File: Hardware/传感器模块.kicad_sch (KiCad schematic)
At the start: 1 part, among them U2 AHT20

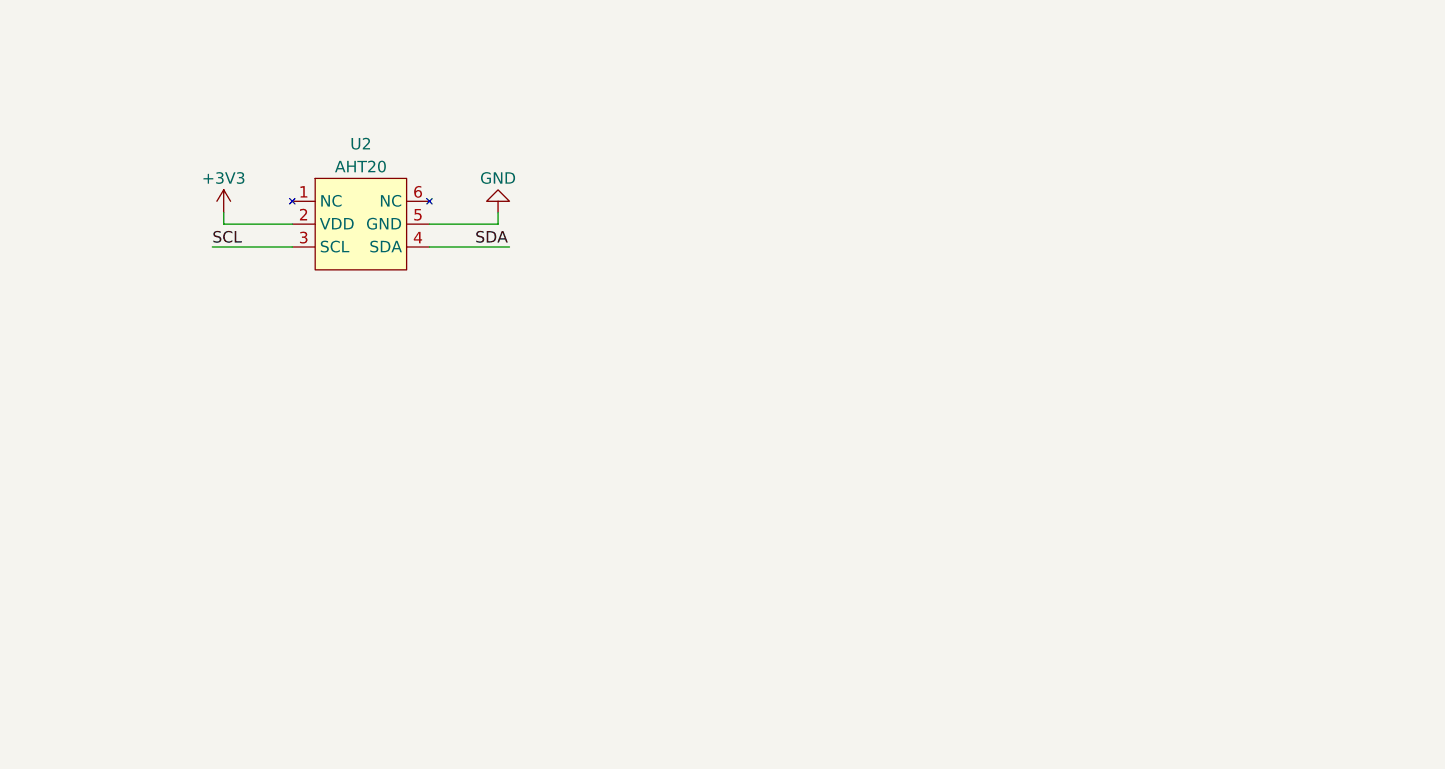
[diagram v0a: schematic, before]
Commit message: 完成传感器模块原理图
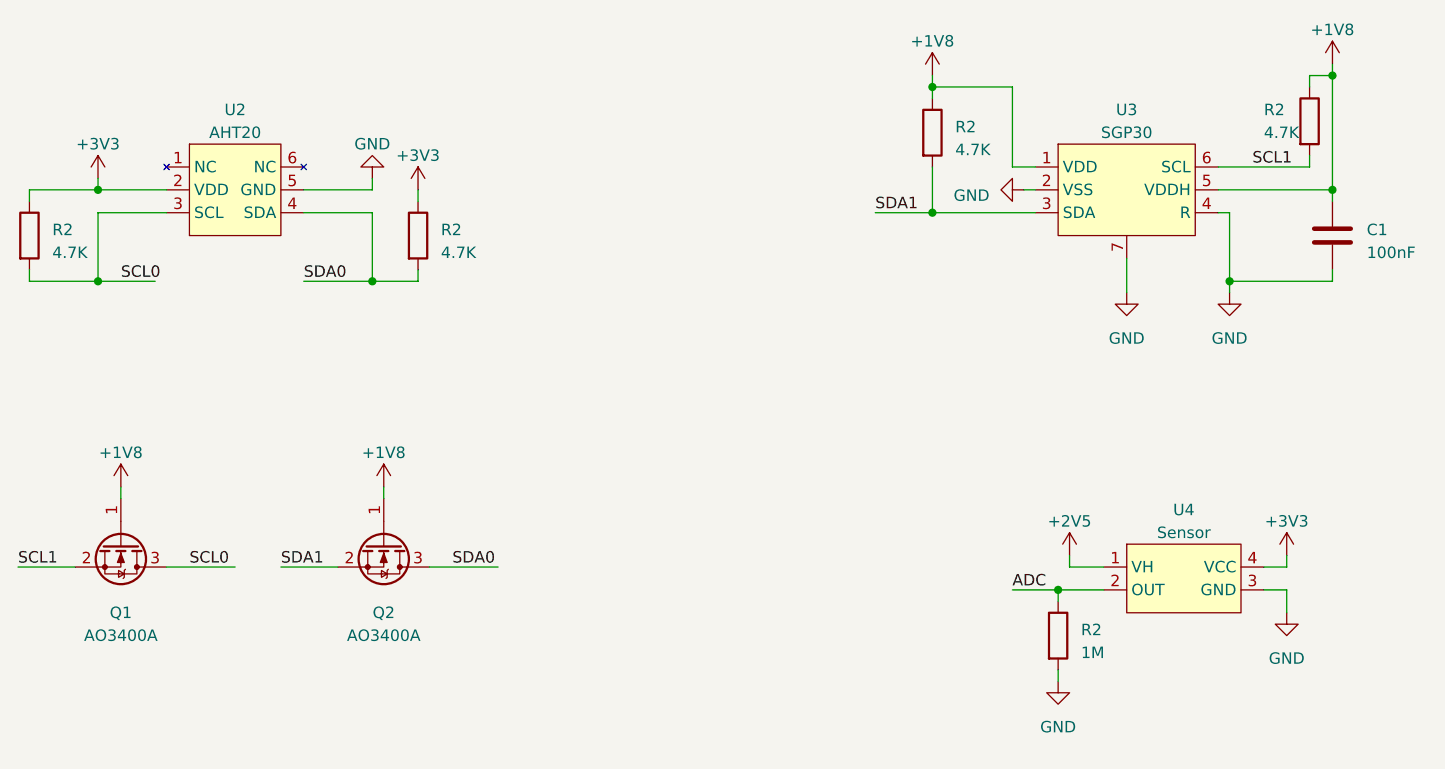
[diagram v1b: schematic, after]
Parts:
- added C1: 100nF, symbol Device:C
- added Q1, Q2: AO3400A, Package_TO_SOT_SMD:SOT-23, symbol Transistor_FET:AO3400A
- added R2 (x4): 4.7K, symbol Device:R
- added R2: 1M, symbol Device:R
- added U3: SGP30, My_Sensor:SGP30, symbol My_Sensor:SGP30
- added U4: Sensor, My_Sensor:MEMS气体传感器, symbol My_Sensor:MEMS气体传感器_乙醇
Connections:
- net +3V3: now also R2.1, R2.1, U4.4 (VCC)
- net GND: now also C1.2, R2.2, U3.2 (VSS), U3.4 (R), U3.7, U4.3 (GND)
- net SCL renamed SCL0
- net SCL0: now also Q1.3 (D), R2.2
- net SDA renamed SDA0
- net SDA0: now also Q2.3 (D), R2.2
- new net +1V8: C1.1, Q1.1 (G), Q2.1 (G), R2.1, R2.1, U3.1 (VDD), U3.5 (VDDH)
- new net +2V5: U4.1 (VH)
- new net ADC: R2.1, U4.2 (OUT)
- new net SCL1: Q1.2 (S), R2.2, U3.6 (SCL)
- new net SDA1: Q2.2 (S), R2.2, U3.3 (SDA)
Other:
- moved on the sheet: U2

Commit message: 2023/3/29
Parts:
- C1: value 100nF -> 104; footprint (none) -> Capacitor_SMD:C_0402_1005Metric
- R2: footprint (none) -> Resistor_SMD:R_0402_1005Metric
- renumbered U3 to U10, U4 to U11, U2 to U9
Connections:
- net SCL0 renamed SCL
- net SCL1 renamed SCL1V8
- net SDA0 renamed SDA
- net SDA1 renamed SDA1V8
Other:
- moved on the sheet: C1, Q1, Q2, R2

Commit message: nm
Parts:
- renumbered U9 to U7, U10 to U8, U11 to U9
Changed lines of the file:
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@@
         )
         (path "/2599b9a9-6312-402b-9c24-1e87744a4c70/43eb1204-8bf3-4d5b-873c-7d8df09b6f9d"
-          (reference "R9") (unit 1)
+          (reference "R16") (unit 1)
         )
       )
@@
         )
         (path "/2599b9a9-6312-402b-9c24-1e87744a4c70/43eb1204-8bf3-4d5b-873c-7d8df09b6f9d"
-          (reference "R10") (unit 1)
+          (reference "R17") (unit 1)
         )
       )
@@
         )
         (path "/2599b9a9-6312-402b-9c24-1e87744a4c70/43eb1204-8bf3-4d5b-873c-7d8df09b6f9d"
-          (reference "#PWR060") (unit 1)
+          (reference "#PWR062") (unit 1)
         )
       )
@@
         )
         (path "/2599b9a9-6312-402b-9c24-1e87744a4c70/43eb1204-8bf3-4d5b-873c-7d8df09b6f9d"
-          (reference "#PWR062") (unit 1)
+          (reference "#PWR064") (unit 1)
         )
       )
@@
         )
         (path "/2599b9a9-6312-402b-9c24-1e87744a4c70/43eb1204-8bf3-4d5b-873c-7d8df09b6f9d"
-          (reference "R11") (unit 1)
+          (reference "R18") (unit 1)
         )
       )
@@
   (symbol (lib_id "My_Sensor:MEMS气体传感器_乙醇") (at 196.85 105.41 0) (unit 1)
     (in_bom yes) (on_board yes) (dnp no) (fields_autoplaced)
-    (property "Reference" "U11" (at 196.85 97.79 0)
+    (property "Reference" "U9" (at 196.85 97.79 0)
       (effects (font (size 1.27 1.27)))
     )
@@
       (project "Warehouse-on-STM32"
         (path "/2599b9a9-6312-402b-9c24-1e87744a4c70/43eb1204-8bf3-4d5b-873c-7d8df09b6f9d"
-          (reference "U11") (unit 1)
+          (reference "U9") (unit 1)
         )
       )
@@
   (symbol (lib_id "power:+1V8") (at 91.44 106.68 0) (unit 1)
     (in_bom yes) (on_board yes) (dnp no) (fields_autoplaced)
-    (property "Reference" "#PWR052" (at 91.44 110.49 0)
+    (property "Reference" "#PWR054" (at 91.44 110.49 0)
       (effects (font (size 1.27 1.27)) hide)
     )
@@
       (project "Warehouse-on-STM32"
         (path "/2599b9a9-6312-402b-9c24-1e87744a4c70/43eb1204-8bf3-4d5b-873c-7d8df09b6f9d"
-          (reference "#PWR052") (unit 1)
+          (reference "#PWR054") (unit 1)
         )
       )
@@
         )
         (path "/2599b9a9-6312-402b-9c24-1e87744a4c70/43eb1204-8bf3-4d5b-873c-7d8df09b6f9d"
-          (reference "#PWR056") (unit 1)
+          (reference "#PWR058") (unit 1)
         )
       )
@@
         )
         (path "/2599b9a9-6312-402b-9c24-1e87744a4c70/43eb1204-8bf3-4d5b-873c-7d8df09b6f9d"
-          (reference "R12") (unit 1)
+          (reference "R19") (unit 1)
         )
       )
@@
   (symbol (lib_id "power:+1V8") (at 91.44 82.55 0) (unit 1)
     (in_bom yes) (on_board yes) (dnp no) (fields_autoplaced)
-    (property "Reference" "#PWR051" (at 91.44 86.36 0)
+    (property "Reference" "#PWR053" (at 91.44 86.36 0)
       (effects (font (size 1.27 1.27)) hide)
     )
@@
       (project "Warehouse-on-STM32"
         (path "/2599b9a9-6312-402b-9c24-1e87744a4c70/43eb1204-8bf3-4d5b-873c-7d8df09b6f9d"
-          (reference "#PWR051") (unit 1)
+          (reference "#PWR053") (unit 1)
         )
       )
@@
         )
         (path "/2599b9a9-6312-402b-9c24-1e87744a4c70/43eb1204-8bf3-4d5b-873c-7d8df09b6f9d"
-          (reference "#PWR053") (unit 1)
+          (reference "#PWR055") (unit 1)
         )
       )
@@
         )
         (path "/2599b9a9-6312-402b-9c24-1e87744a4c70/43eb1204-8bf3-4d5b-873c-7d8df09b6f9d"
-          (reference "R13") (unit 1)
+          (reference "R20") (unit 1)
         )
       )
@@
   (symbol (lib_id "power:+1V8") (at 168.91 49.53 0) (unit 1)
     (in_bom yes) (on_board yes) (dnp no) (fields_autoplaced)
-    (property "Reference" "#PWR055" (at 168.91 53.34 0)
+    (property "Reference" "#PWR057" (at 168.91 53.34 0)
       (effects (font (size 1.27 1.27)) hide)
     )
@@
       (project "Warehouse-on-STM32"
         (path "/2599b9a9-6312-402b-9c24-1e87744a4c70/43eb1204-8bf3-4d5b-873c-7d8df09b6f9d"
-          (reference "#PWR055") (unit 1)
+          (reference "#PWR057") (unit 1)
         )
       )
@@
         )
         (path "/2599b9a9-6312-402b-9c24-1e87744a4c70/43eb1204-8bf3-4d5b-873c-7d8df09b6f9d"
-          (reference "#PWR057") (unit 1)
+          (reference "#PWR059") (unit 1)
         )
       )
@@
         )
         (path "/2599b9a9-6312-402b-9c24-1e87744a4c70/43eb1204-8bf3-4d5b-873c-7d8df09b6f9d"
+          (reference "#PWR063") (unit 1)
+        )
+      )
+    )
+  )
+  (symbol (lib_id "power:GND") (at 190.5 73.66 0) (unit 1)
+    (in_bom yes) (on_board yes) (dnp no) (fields_autoplaced)
+    (property "Reference" "#PWR04" (at 190.5 80.01 0)
+      (effects (font (size 1.27 1.27)) hide)
+    )
+    (property "Value" "GND" (at 190.5 78.74 0)
+      (effects (font (size 1.27 1.27)))
+    )
+    (property "Footprint" "" (at 190.5 73.66 0)
+      (effects (font (size 1.27 1.27)) hide)
+    )
+    (property "Datasheet" "" (at 190.5 73.66 0)
+      (effects (font (size 1.27 1.27)) hide)
+    )
+    (pin "1")
+    (instances
+      (project "Warehouse-on-STM32"
+        (path "/2599b9a9-6312-402b-9c24-1e87744a4c70"
+          (reference "#PWR04") (unit 1)
+        )
+        (path "/2599b9a9-6312-402b-9c24-1e87744a4c70/43eb1204-8bf3-4d5b-873c-7d8df09b6f9d"
           (reference "#PWR061") (unit 1)
         )
@@
     )
   )
-  (symbol (lib_id "power:GND") (at 190.5 73.66 0) (unit 1)
-    (in_bom yes) (on_board yes) (dnp no) (fields_autoplaced)
-    (property "Reference" "#PWR04" (at 190.5 80.01 0)
-      (effects (font (size 1.27 1.27)) hide)
-    )
-    (property "Value" "GND" (at 190.5 78.74 0)
-      (effects (font (size 1.27 1.27)))
-    )
-    (property "Footprint" "" (at 190.5 73.66 0)
-      (effects (font (size 1.27 1.27)) hide)
-    )
-    (property "Datasheet" "" (at 190.5 73.66 0)
-      (effects (font (size 1.27 1.27)) hide)
-    )
-    (pin "1")
-    (instances
-      (project "Warehouse-on-STM32"
-        (path "/2599b9a9-6312-402b-9c24-1e87744a4c70"
-          (reference "#PWR04") (unit 1)
-        )
-        (path "/2599b9a9-6312-402b-9c24-1e87744a4c70/43eb1204-8bf3-4d5b-873c-7d8df09b6f9d"
-          (reference "#PWR059") (unit 1)
-        )
-      )
-    )
-  )
   (symbol (lib_id "power:+3V3") (at 111.76 62.23 0) (unit 1)
     (in_bom yes) (on_board yes) (dnp no) (fields_autoplaced)
@@
         )
         (path "/2599b9a9-6312-402b-9c24-1e87744a4c70/43eb1204-8bf3-4d5b-873c-7d8df09b6f9d"
-          (reference "#PWR054") (unit 1)
+          (reference "#PWR056") (unit 1)
         )
       )
@@
   (symbol (lib_id "My_Sensor:AHT20") (at 91.44 62.23 0) (unit 1)
     (in_bom yes) (on_board yes) (dnp no) (fields_autoplaced)
-    (property "Reference" "U9" (at 91.44 53.34 0)
+    (property "Reference" "U7" (at 91.44 53.34 0)
       (effects (font (size 1.27 1.27)))
     )
@@
       (project "Warehouse-on-STM32"
         (path "/2599b9a9-6312-402b-9c24-1e87744a4c70/43eb1204-8bf3-4d5b-873c-7d8df09b6f9d"
-          (reference "U9") (unit 1)
+          (reference "U7") (unit 1)
         )
       )
@@
         )
         (path "/2599b9a9-6312-402b-9c24-1e87744a4c70/43eb1204-8bf3-4d5b-873c-7d8df09b6f9d"
-          (reference "#PWR050") (unit 1)
+          (reference "#PWR052") (unit 1)
         )
       )
@@
   (symbol (lib_id "My_Sensor:SGP30") (at 190.5 62.23 0) (unit 1)
     (in_bom yes) (on_board yes) (dnp no) (fields_autoplaced)
-    (property "Reference" "U10" (at 190.5 53.34 0)
+    (property "Reference" "U8" (at 190.5 53.34 0)
       (effects (font (size 1.27 1.27)))
     )
@@
       (project "Warehouse-on-STM32"
         (path "/2599b9a9-6312-402b-9c24-1e87744a4c70/43eb1204-8bf3-4d5b-873c-7d8df09b6f9d"
-          (reference "U10") (unit 1)
+          (reference "U8") (unit 1)
         )
       )
@@
   (symbol (lib_id "power:+2V5") (at 184.15 102.87 0) (unit 1)
     (in_bom yes) (on_board yes) (dnp no) (fields_autoplaced)
-    (property "Reference" "#PWR058" (at 184.15 106.68 0)
+    (property "Reference" "#PWR060" (at 184.15 106.68 0)
       (effects (font (size 1.27 1.27)) hide)
     )
@@
       (project "Warehouse-on-STM32"
         (path "/2599b9a9-6312-402b-9c24-1e87744a4c70/43eb1204-8bf3-4d5b-873c-7d8df09b6f9d"
-          (reference "#PWR058") (unit 1)
+          (reference "#PWR060") (unit 1)
         )
       )
@@
   (symbol (lib_id "power:+1V8") (at 214.63 48.26 0) (unit 1)
     (in_bom yes) (on_board yes) (dnp no) (fields_autoplaced)
-    (property "Reference" "#PWR063" (at 214.63 52.07 0)
+    (property "Reference" "#PWR065" (at 214.63 52.07 0)
       (effects (font (size 1.27 1.27)) hide)
     )
@@
       (project "Warehouse-on-STM32"
         (path "/2599b9a9-6312-402b-9c24-1e87744a4c70/43eb1204-8bf3-4d5b-873c-7d8df09b6f9d"
-          (reference "#PWR063") (unit 1)
-        )
-      )
+          (reference "#PWR065") (unit 1)
+        )
+      )

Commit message: 完成布局
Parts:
- U7: footprint My_Sensor:AHT20 -> Sensor:AHT20
- U8: footprint My_Sensor:SGP30 -> Sensor:SGP30
- U9: footprint My_Sensor:MEMS气体传感器 -> Sensor:MEMS气体传感器
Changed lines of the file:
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@@
       (effects (font (size 1.27 1.27)))
     )
-    (property "Footprint" "My_Sensor:MEMS气体传感器" (at 196.85 110.49 0)
+    (property "Footprint" "Sensor:MEMS气体传感器" (at 196.85 110.49 0)
       (effects (font (size 1.27 1.27)) hide)
     )
@@
       (effects (font (size 1.27 1.27)))
     )
-    (property "Footprint" "My_Sensor:AHT20" (at 96.52 63.5 0)
+    (property "Footprint" "Sensor:AHT20" (at 96.52 63.5 0)
       (effects (font (size 1.27 1.27)) hide)
     )
@@
       (effects (font (size 1.27 1.27)))
     )
-    (property "Footprint" "My_Sensor:SGP30" (at 199.39 72.39 0)
-      (effects (font (size 1.27 1.27)) hide)
-    )
+    (property "Footprint" "Sensor:SGP30" (at 199.39 72.39 0)
+      (effects (font (size 1.27 1.27)) hide)
+    )
